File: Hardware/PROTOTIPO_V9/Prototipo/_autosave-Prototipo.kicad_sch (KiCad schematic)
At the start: 1 part, among them U1 YAAJ_BluePill_Part_Like_SWD_B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

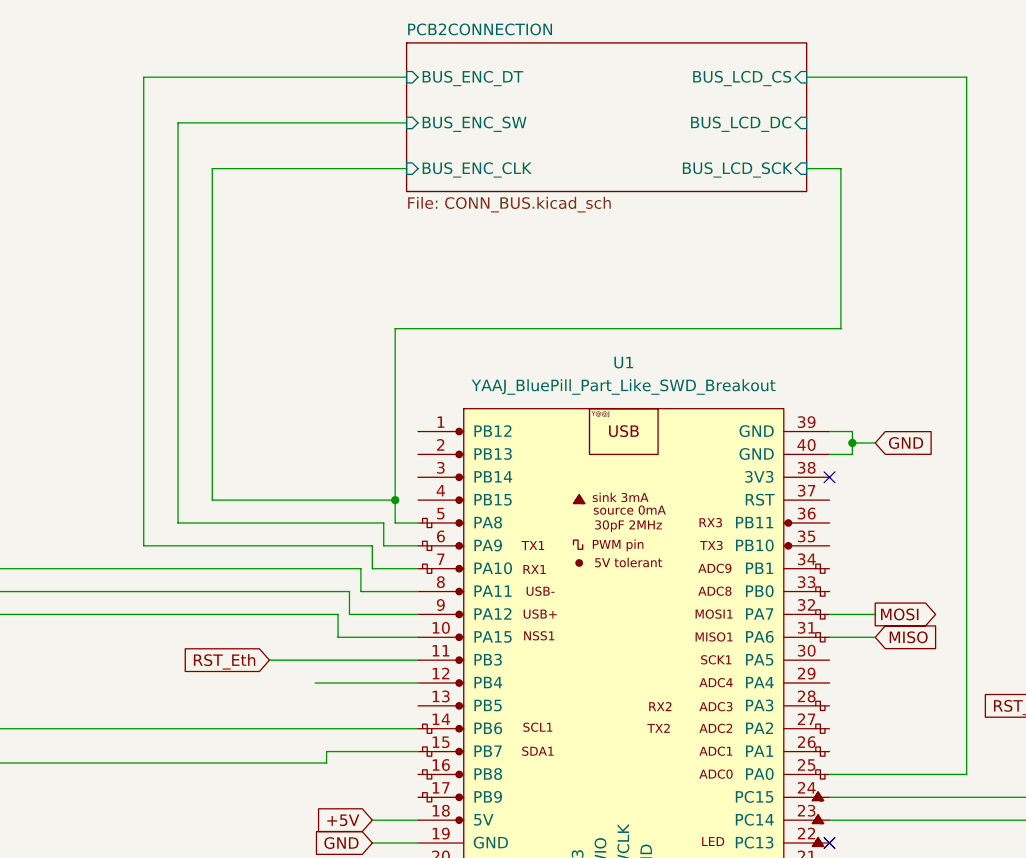
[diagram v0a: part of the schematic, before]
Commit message: sch ILI9341
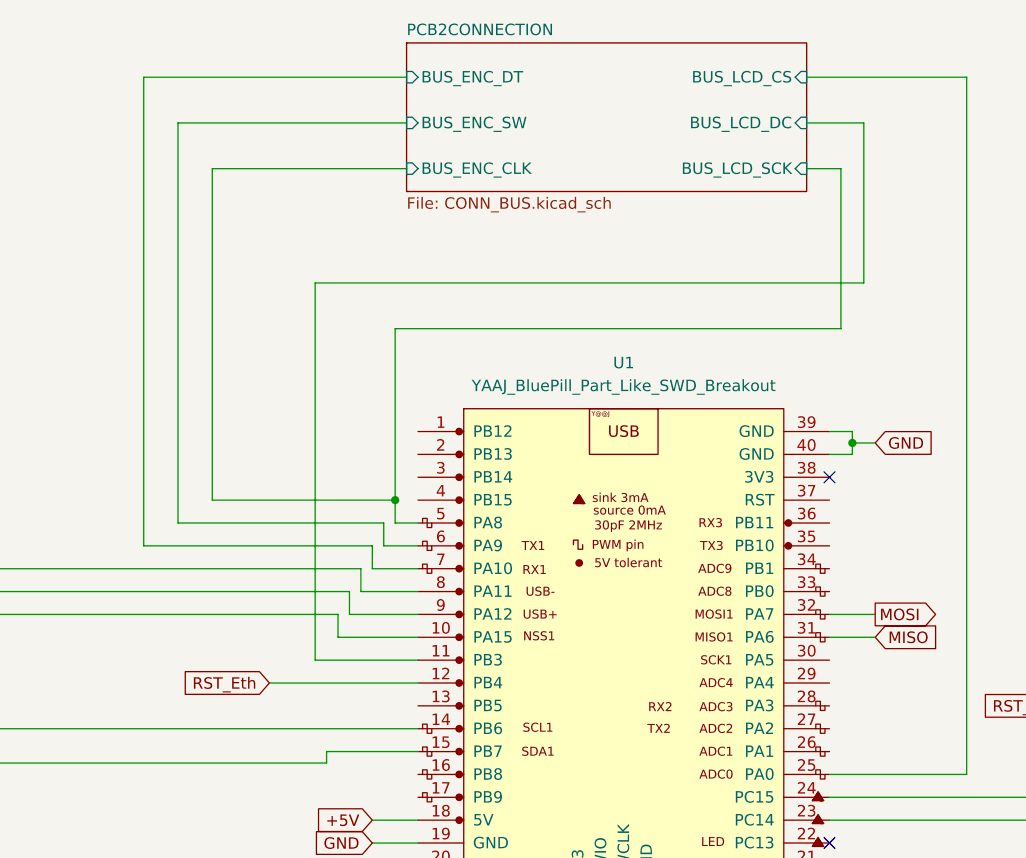
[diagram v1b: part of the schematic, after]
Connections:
- net PCB2CONNECTION/BUS_LCD_DC: now also U1.11 (PB3)
- net RST_Eth: now also U1.12 (PB4); no longer U1.11 (PB3)
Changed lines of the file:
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@@
+	(wire
+		(pts
+			(xy 173.99 41.91) (xy 173.99 59.69)
+		)
+		(stroke
+			(width 0)
+			(type default)
+		)
+	)
 	(wire
 		(pts
@@
 	(wire
 		(pts
+			(xy 113.03 59.69) (xy 113.03 101.6)
+		)
+		(stroke
+			(width 0)
+			(type default)
+		)
+	)
+	(wire
+		(pts
 			(xy 121.92 86.36) (xy 124.46 86.36)
 		)
@@
 	(wire
 		(pts
+			(xy 113.03 101.6) (xy 124.46 101.6)
+		)
+		(stroke
+			(width 0)
+			(type default)
+		)
+	)
+	(wire
+		(pts
 			(xy 149.86 135.89) (xy 149.86 132.08)
 		)
@@
 	(wire
 		(pts
-			(xy 107.95 101.6) (xy 124.46 101.6)
+			(xy 107.95 104.14) (xy 124.46 104.14)
 		)
 		(stroke
@@
 	(wire
 		(pts
+			(xy 173.99 59.69) (xy 113.03 59.69)
+		)
+		(stroke
+			(width 0)
+			(type default)
+		)
+	)
+	(wire
+		(pts
 			(xy 118.11 93.98) (xy 124.46 93.98)
 		)
@@
 	(wire
 		(pts
-			(xy 113.03 104.14) (xy 124.46 104.14)
-		)
-		(stroke
-			(width 0)
-			(type default)
-		)
-	)
-	(wire
-		(pts
 			(xy 33.02 49.53) (xy 36.83 49.53)
 		)
@@
 		(pts
 			(xy 170.18 76.2) (xy 172.72 76.2)
+		)
+		(stroke
+			(width 0)
+			(type default)
+		)
+	)
+	(wire
+		(pts
+			(xy 167.64 41.91) (xy 173.99 41.91)
 		)
 		(stroke
@@
 	(global_label "RST_Eth"
 		(shape input)
-		(at 107.95 101.6 180)
+		(at 107.95 104.14 180)
 		(fields_autoplaced yes)
 		(effects
@@
 		)
 		(property "Intersheetrefs" "${INTERSHEET_REFS}"
-			(at 97.5264 101.6 0)
+			(at 97.5264 104.14 0)
 			(effects
 				(font
